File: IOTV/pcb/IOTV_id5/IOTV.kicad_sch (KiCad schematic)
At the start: 22 parts, among them J1 Screw_Terminal_01x02, J2 Screw_Terminal_01x02, J3 Conn_01x04, J4 Conn_01x04, J5 Conn_01x04, J6 Conn_01x05, K1 TIANBO-HJR-4102-L, Q1 MMBT3904, U1 ESP32_DevKit_V1_DOIT

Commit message: id-5 pcb
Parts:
- Q1: value MMBT3904 -> S9013
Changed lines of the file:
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@@
       (effects (font (size 1.27 1.27)))
     )
-    (property "Value" "MMBT3904" (at 177.8 67.31 90)
+    (property "Value" "S9013" (at 177.8 67.31 90)
       (effects (font (size 1.27 1.27)))
     )

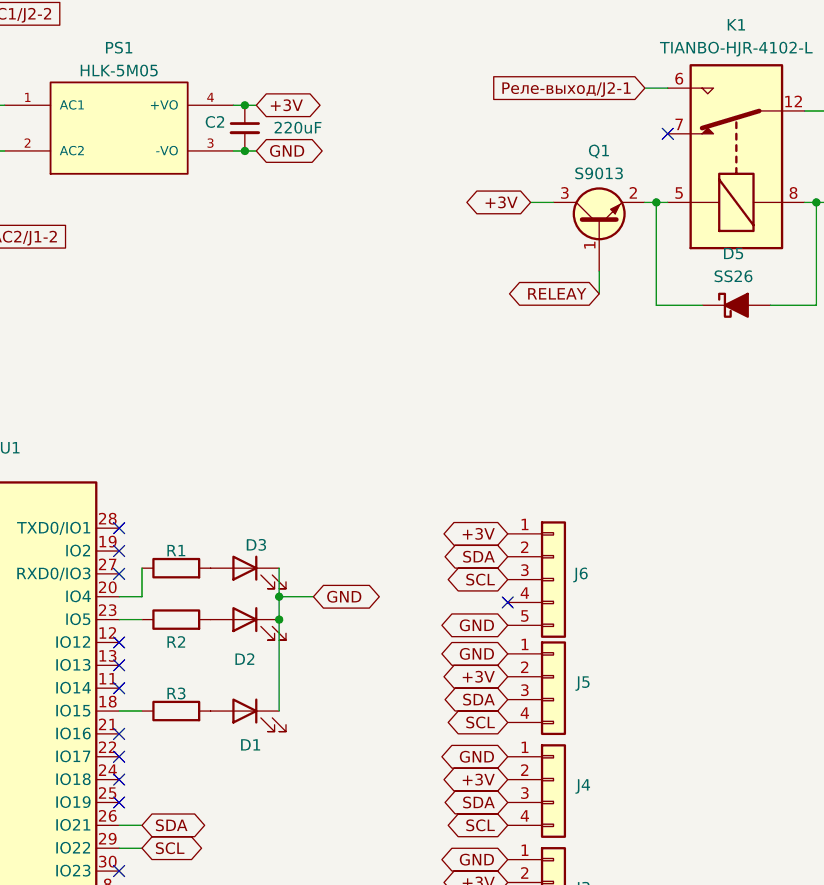
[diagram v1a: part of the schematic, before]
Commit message: pcb id5 маркировки номиналов резисторов
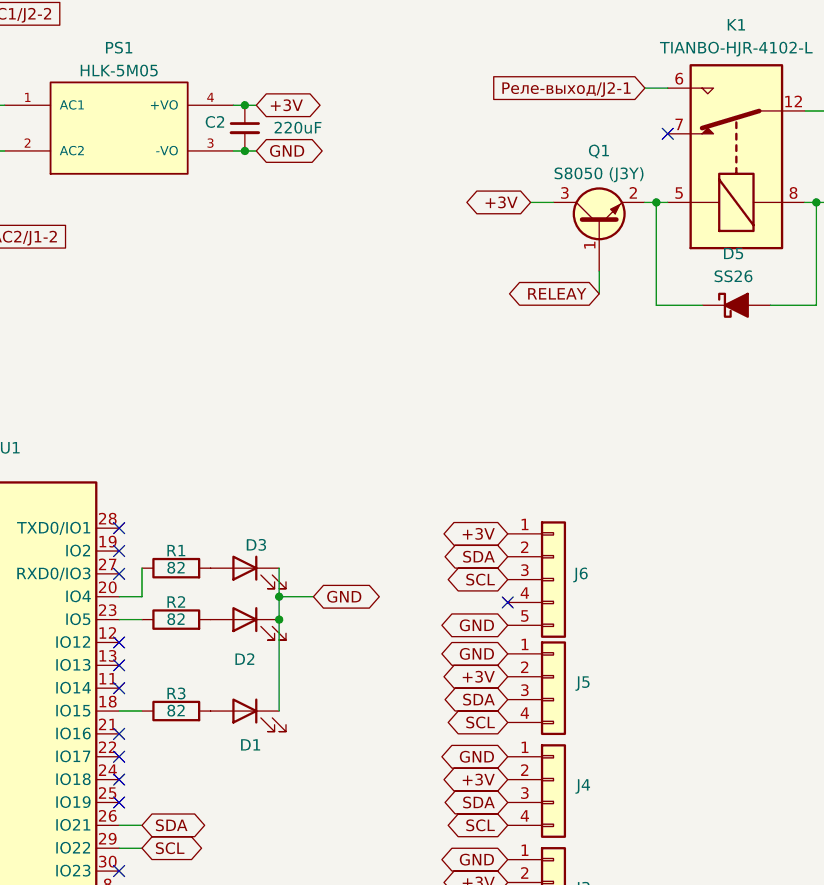
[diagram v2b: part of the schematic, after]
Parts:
- Q1: value S9013 -> S8050 (J3Y)
- R1, R2, R3: value 0R_0603 -> 82
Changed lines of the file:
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@@
       (effects (font (size 1.27 1.27)))
     )
-    (property "Value" "0R_0603" (at 130.81 129.54 90)
-      (effects (font (size 1.27 1.27)) hide)
+    (property "Value" "82" (at 130.81 127 90)
+      (effects (font (size 1.27 1.27)))
     )
     (property "Footprint" "PCM_Resistor_SMD_AKL:R_1206_3216Metric" (at 143.51 129.54 0)
@@
   (symbol (lib_id "PCM_4ms_Resistor:0R_0603") (at 130.81 116.84 90) (unit 1)
     (in_bom yes) (on_board yes) (dnp no)
-    (property "Reference" "R2" (at 130.81 119.38 90)
-      (effects (font (size 1.27 1.27)))
-    )
-    (property "Value" "0R_0603" (at 130.81 119.38 90)
-      (effects (font (size 1.27 1.27)) hide)
+    (property "Reference" "R2" (at 130.81 114.935 90)
+      (effects (font (size 1.27 1.27)))
+    )
+    (property "Value" "82" (at 130.81 116.84 90)
+      (effects (font (size 1.27 1.27)))
     )
     (property "Footprint" "PCM_Resistor_SMD_AKL:R_1206_3216Metric" (at 143.51 119.38 0)
@@
       (effects (font (size 1.27 1.27)))
     )
-    (property "Value" "S9013" (at 177.8 67.31 90)
+    (property "Value" "S8050 (J3Y)" (at 177.8 67.31 90)
       (effects (font (size 1.27 1.27)))
     )
@@
       (effects (font (size 1.27 1.27)))
     )
-    (property "Value" "0R_0603" (at 130.81 113.665 90)
-      (effects (font (size 1.27 1.27)) hide)
+    (property "Value" "82" (at 130.81 111.125 90)
+      (effects (font (size 1.27 1.27)))
     )
     (property "Footprint" "PCM_Resistor_SMD_AKL:R_1206_3216Metric" (at 143.51 113.665 0)

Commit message: PCB id5
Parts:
- removed D1, D2, D3: LED, LED_SMD:LED_0603_1608Metric, symbol Device:LED
- removed D5: SS26, Diode_SMD:D_SMB, symbol PCM_Diode_Schottky_AKL:SS26
- removed K1: TIANBO-HJR-4102-L, Relay_THT:Relay_SPDT_HJR-4102, symbol Relay:TIANBO-HJR-4102-L
- removed Q1: S8050 (J3Y), Package_TO_SOT_SMD:SOT-23, symbol PCM_Transistor_BJT_AKL:MMBT3904
- removed R1, R2, R3: 82, PCM_Resistor_SMD_AKL:R_1206_3216Metric, symbol PCM_4ms_Resistor:0R_0603
- removed U1: ESP32_DevKit_V1_DOIT, esp32_devkit_v1_doit:esp32_devkit_v1_doit, symbol esp32_devkit_v1_doit:ESP32_DevKit_V1_DOIT
- added C1, C2, C3, C4: C_Generic, Capacitor_SMD:C_1206_3216Metric, symbol PCM_4ms_Capacitor:C_Generic
- added J7: JTAG, Connector_PinHeader_2.54mm:PinHeader_1x04_P2.54mm_Vertical, symbol Connector_Generic:Conn_01x04
- added J8: UART, Connector_PinHeader_2.54mm:PinHeader_1x04_P2.54mm_Vertical, symbol Connector_Generic:Conn_01x04
- added R1: 10K, Resistor_SMD:R_1206_3216Metric, symbol Device:R
- added R2: ?, Resistor_SMD:R_1206_3216Metric, symbol Device:R
- added SW1: RST, Button_Switch_SMD:SW_SPST_TL3342, symbol Switch:SW_Push
- added SW2: Boot, Button_Switch_SMD:SW_SPST_TL3342, symbol Switch:SW_Push
- added U1: ESP32-WROOM-E, Espressif:ESP32-WROOM-32E, symbol Espressif:ESP32-WROOM-E
- added U2: G7DA-28 (Z)D3 8A/240V (3-32V), OptoDevice:Finder_34.81, symbol Relay_SolidState:34.81-7048
- PS1: footprint Converter_ACDC:CONV_HLK-5M05 -> HLK-5M05:CONV_HLK-5M05
- renumbered C1 to C5, C2 to C6
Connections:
- net GND: now also C1.2, C2.2, C3.2, C4.2, J8.4 (Pin_4), SW1.2, SW2.2, U1.1 (GND), U1.15 (GND), U1.38 (GND), U1.39 (GND_THERMAL), U2.A2
- net SCL: now also U1.36 (GPIO22)
- net SDA: now also U1.33 (GPIO21)
- net +3V renamed +3.3V
- net +3.3V: now also C1.1, C2.1, J8.1 (Pin_1), R1.1, U1.2 (3V3)
- net HLK-AC1/J2-2: no longer names the net of FL1.1, PS1.2 (AC2)
- net HLK-AC2/J1-2: no longer names the net of FL1.4, PS1.1 (AC1)
- net J1-1/J2-1: no longer names the net of F1.1, J1.1 (Pin_1), J2.1 (Pin_1)
- net J1-2 renamed SSD-1
- net SSD-1: now also U2.11
- net Реле-выход/J2-1 renamed SSD-2
- net SSD-2: now also U2.14
- new net: C4.1, R2.1, SW1.1
- new net EN: C3.1, R1.2, R2.2, U1.3 (EN/CHIP_PU)
- new net GPIO0: SW2.1, U1.25 (GPIO0/BOOT/ADC2_CH1)
- new net GPIO34: U1.6 (GPIO34/ADC1_CH6), U2.A1
- new net TCK: J7.3 (Pin_3), U1.16 (MTCK/GPIO13/ADC2_CH4)
- new net TDI: J7.2 (Pin_2), U1.14 (MTDI/GPIO12/ADC2_CH5)
- new net TDO: J7.4 (Pin_4), U1.23 (MTDO/GPIO15/ADC2_CH3)
- new net TMS: J7.1 (Pin_1), U1.13 (MTMS/GPIO14/ADC2_CH6)
- new net U0RX: J8.3 (Pin_3), U1.34 (U0RXD/GPIO3)
- new net U0TX: J8.2 (Pin_2), U1.35 (U0TXD/GPIO1)
- no-connect marks 23 -> 17
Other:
- moved on the sheet: J3, J4, J5, J6

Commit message: pcb id5 rev1.2
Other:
- moved on the sheet: C1, C2, C3, C4, C5, C6, F1, FL1, J1, J2, J3, J4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

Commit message: pcb id5 rev 1.2
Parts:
- removed J7: JTAG, Connector_PinHeader_2.54mm:PinHeader_1x04_P2.54mm_Vertical, symbol Connector_Generic:Conn_01x04
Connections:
- net +3.3V: now also J8.4 (Pin_4); no longer J8.1 (Pin_1)
- net GND: now also J8.1 (Pin_1); no longer J8.4 (Pin_4)
- net U0RX: now also J8.2 (Pin_2); no longer J8.3 (Pin_3)
- net U0TX: now also J8.3 (Pin_3); no longer J8.2 (Pin_2)
- net at FL1.1: now also PS1.1 (AC1); no longer PS1.2 (AC2)
- net at FL1.4: now also PS1.2 (AC2); no longer PS1.1 (AC1)
- net TCK: no longer names the net of U1.16 (MTCK/GPIO13/ADC2_CH4)
- net TDI: no longer names the net of U1.14 (MTDI/GPIO12/ADC2_CH5)
- net TDO: no longer names the net of U1.23 (MTDO/GPIO15/ADC2_CH3)
- net TMS: no longer names the net of U1.13 (MTMS/GPIO14/ADC2_CH6)
- no-connect marks 17 -> 21
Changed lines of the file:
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@@
     (title "IOTV id-5")
     (date "2023-04-21")
+    (rev "3")
     (company "Вербкин М.С.")
   )
@@
   (junction (at 150.368 39.37) (diameter 0) (color 0 0 0 0)
   )
+  (no_connect (at 76.2 93.345))
+  (no_connect (at 76.2 95.885))
   (no_connect (at 142.24 88.265))
   (no_connect (at 76.2 106.045))
@@
   (no_connect (at 142.24 95.885))
   (no_connect (at 142.24 93.345))
+  (no_connect (at 76.2 90.805))
   (no_connect (at 142.24 98.425))
   (no_connect (at 142.24 118.745))
+  (no_connect (at 76.2 98.425))
   (no_connect (at 142.24 90.805))
   (no_connect (at 76.2 83.185))
@@
     (stroke (width 0) (type default))
   )
-  (wire (pts (xy 99.568 34.29) (xy 116.078 34.29))
-    (stroke (width 0) (type default))
-  )
   (wire (pts (xy 149.098 39.37) (xy 150.368 39.37))
     (stroke (width 0) (type default))
   )
-  (wire (pts (xy 121.158 44.45) (xy 121.158 34.29))
-    (stroke (width 0) (type default))
-  )
-  (wire (pts (xy 121.158 34.29) (xy 123.698 34.29))
-    (stroke (width 0) (type default))
-  )
   (wire (pts (xy 66.04 66.675) (xy 66.04 68.58))
     (stroke (width 0) (type default))
@@
     (stroke (width 0) (type default))
   )
-  (wire (pts (xy 116.078 34.29) (xy 116.078 39.37))
-    (stroke (width 0) (type default))
-  )
   (wire (pts (xy 77.343 51.435) (xy 77.978 51.435))
     (stroke (width 0) (type default))
   )
-  (wire (pts (xy 109.728 44.45) (xy 121.158 44.45))
+  (wire (pts (xy 99.568 34.29) (xy 123.698 34.29))
+    (stroke (width 0) (type default))
+  )
+  (wire (pts (xy 109.728 44.45) (xy 123.698 44.45))
     (stroke (width 0) (type default))
   )
@@
     (stroke (width 0) (type default))
   )
+  (wire (pts (xy 123.698 44.45) (xy 123.698 39.37))
+    (stroke (width 0) (type default))
+  )
   (wire (pts (xy 64.135 83.185) (xy 64.135 86.995))
     (stroke (width 0) (type default))
   )
-  (wire (pts (xy 116.078 39.37) (xy 123.698 39.37))
-    (stroke (width 0) (type default))
-  )
   (wire (pts (xy 111.76 125.73) (xy 109.22 125.73))
     (stroke (width 0) (type default))
@@
     )
   )
-  (global_label "TDO" (shape bidirectional) (at 76.2 98.425 180) (fields_autoplaced)
-    (effects (font (size 1.27 1.27)) (justify right))
-    (property "Intersheetrefs" "${INTERSHEET_REFS}" (at 68.6148 98.425 0)
-      (effects (font (size 1.27 1.27)) (justify right))
-    )
-  )
   (global_label "GND" (shape bidirectional) (at 192.405 91.44 180) (fields_autoplaced)
     (effects (font (size 1.27 1.27)) (justify right))
@@
     )
   )
-  (global_label "TCK" (shape bidirectional) (at 76.2 93.345 180) (fields_autoplaced)
-    (effects (font (size 1.27 1.27)) (justify right))
-    (property "Intersheetrefs" "${INTERSHEET_REFS}" (at 68.6753 93.345 0)
-      (effects (font (size 1.27 1.27)) (justify right))
-    )
-  )
-  (global_label "U0TX" (shape bidirectional) (at 43.18 141.605 180) (fields_autoplaced)
-    (effects (font (size 1.27 1.27)) (justify right))
-    (property "Intersheetrefs" "${INTERSHEET_REFS}" (at 34.4458 141.605 0)
+  (global_label "U0TX" (shape bidirectional) (at 43.18 144.145 180) (fields_autoplaced)
+    (effects (font (size 1.27 1.27)) (justify right))
+    (property "Intersheetrefs" "${INTERSHEET_REFS}" (at 34.4458 144.145 0)
       (effects (font (size 1.27 1.27)) (justify right))
     )
@@
     )
   )
-  (global_label "TMS" (shape bidirectional) (at 76.2 95.885 180) (fields_autoplaced)
-    (effects (font (size 1.27 1.27)) (justify right))
-    (property "Intersheetrefs" "${INTERSHEET_REFS}" (at 68.5544 95.885 0)
-      (effects (font (size 1.27 1.27)) (justify right))
-    )
-  )
   (global_label "SCL" (shape bidirectional) (at 192.405 83.185 180) (fields_autoplaced)
     (effects (font (size 1.27 1.27)) (justify right))
@@
     )
   )
-  (global_label "U0RX" (shape bidirectional) (at 43.18 144.145 180) (fields_autoplaced)
-    (effects (font (size 1.27 1.27)) (justify right))
-    (property "Intersheetrefs" "${INTERSHEET_REFS}" (at 34.1434 144.145 0)
+  (global_label "U0RX" (shape bidirectional) (at 43.18 141.605 180) (fields_autoplaced)
+    (effects (font (size 1.27 1.27)) (justify right))
+    (property "Intersheetrefs" "${INTERSHEET_REFS}" (at 34.1434 141.605 0)
       (effects (font (size 1.27 1.27)) (justify right))
     )
@@
     )
   )
-  (global_label "TDI" (shape bidirectional) (at 43.434 125.603 180) (fields_autoplaced)
-    (effects (font (size 1.27 1.27)) (justify right))
-    (property "Intersheetrefs" "${INTERSHEET_REFS}" (at 36.5745 125.603 0)
-      (effects (font (size 1.27 1.27)) (justify right))
-    )
-  )
-  (global_label "TDI" (shape bidirectional) (at 76.2 90.805 180) (fields_autoplaced)
-    (effects (font (size 1.27 1.27)) (justify right))
-    (property "Intersheetrefs" "${INTERSHEET_REFS}" (at 69.3405 90.805 0)
-      (effects (font (size 1.27 1.27)) (justify right))
-    )
-  )
-  (global_label "TDO" (shape bidirectional) (at 43.434 130.683 180) (fields_autoplaced)
-    (effects (font (size 1.27 1.27)) (justify right))
-    (property "Intersheetrefs" "${INTERSHEET_REFS}" (at 35.8488 130.683 0)
-      (effects (font (size 1.27 1.27)) (justify right))
-    )
-  )
   (global_label "SSD-2" (shape input) (at 184.912 31.75 180) (fields_autoplaced)
     (effects (font (size 1.27 1.27)) (justify right))
@@
     )
   )
-  (global_label "TMS" (shape bidirectional) (at 43.434 123.063 180) (fields_autoplaced)
-    (effects (font (size 1.27 1.27)) (justify right))
-    (property "Intersheetrefs" "${INTERSHEET_REFS}" (at 35.7884 123.063 0)
-      (effects (font (size 1.27 1.27)) (justify right))
-    )
-  )
   (global_label "U0RX" (shape bidirectional) (at 142.24 80.645 0) (fields_autoplaced)
     (effects (font (size 1.27 1.27)) (justify left))
@@
     )
   )
-  (global_label "GND" (shape bidirectional) (at 43.18 146.685 180) (fields_autoplaced)
-    (effects (font (size 1.27 1.27)) (justify right))
-    (property "Intersheetrefs" "${INTERSHEET_REFS}" (at 35.2924 146.685 0)
+  (global_label "GND" (shape bidirectional) (at 43.18 139.065 180) (fields_autoplaced)
+    (effects (font (size 1.27 1.27)) (justify right))
+    (property "Intersheetrefs" "${INTERSHEET_REFS}" (at 35.2924 139.065 0)
       (effects (font (size 1.27 1.27)) (justify right))
     )
@@
     )
   )
-  (global_label "+3.3V" (shape bidirectional) (at 43.18 139.065 180) (fields_autoplaced)
-    (effects (font (size 1.27 1.27)) (justify right))
-    (property "Intersheetrefs" "${INTERSHEET_REFS}" (at 33.4781 139.065 0)
+  (global_label "+3.3V" (shape bidirectional) (at 43.18 146.685 180) (fields_autoplaced)
+    (effects (font (size 1.27 1.27)) (justify right))
+    (property "Intersheetrefs" "${INTERSHEET_REFS}" (at 33.4781 146.685 0)
       (effects (font (size 1.27 1.27)) (justify right))
     )
@@
     (effects (font (size 1.27 1.27)) (justify right))
     (property "Intersheetrefs" "${INTERSHEET_REFS}" (at 182.7031 105.41 0)
-      (effects (font (size 1.27 1.27)) (justify right))
-    )
-  )
-  (global_label "TCK" (shape bidirectional) (at 43.434 128.143 180) (fields_autoplaced)
-    (effects (font (size 1.27 1.27)) (justify right))
-    (property "Intersheetrefs" "${INTERSHEET_REFS}" (at 35.9093 128.143 0)
       (effects (font (size 1.27 1.27)) (justify right))
     )
@@
         )
       )
-    )
-  )
-  (symbol (lib_id "Connector_Generic:Conn_01x04") (at 48.514 125.603 0) (unit 1)
-    (in_bom yes) (on_board yes) (dnp no)
-    (property "Reference" "J7" (at 51.689 126.238 0)
-      (effects (font (size 1.27 1.27)) (justify left))
-    )
-    (property "Value" "JTAG" (at 51.689 128.778 0)
-      (effects (font (size 1.27 1.27)) (justify left))
-    )
-    (property "Footprint" "Connector_PinHeader_2.54mm:PinHeader_1x04_P2.54mm_Vertical" (at 48.514 125.603 0)
-      (effects (font (size 1.27 1.27)) hide)
-    )
-    (property "Datasheet" "~" (at 48.514 125.603 0)
-      (effects (font (size 1.27 1.27)) hide)
-    )
-    (pin "1")
-    (pin "2")
-    (pin "3")
-    (pin "4")
-    (instances
-      (project "IOTV"
-        (path "/1ca02c68-d763-4d2d-aed4-975a014c3931"
-          (reference "J7") (unit 1)
-        )
-      )
